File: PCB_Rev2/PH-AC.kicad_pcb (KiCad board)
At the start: 2 copper layers, 200 x 100 mm, 60 parts, among them J1 USB_C_Receptacle_USB2.0_14P, J2 Conn_01x03, Q1 DMG1012T, SW1 SW_Push, SW10 SW_Push, SW2 RotaryEncoder_Switch_MP, SW3 RotaryEncoder_Switch_MP, SW4 SW_Push, SW5 SW_Push, SW6 SW_Push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

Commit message: PCB Modification And Outfit Model Update
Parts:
- moved SW3 4.61 mm to (243.0, 65.6)
- moved SW2 4.24 mm to (77.0, 65.6)
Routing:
- net ENC2B: track 67.6 -> 62.8 mm
- net ENC2A: track 68.8 -> 64.1 mm
- net ENC1B: track 133.6 -> 129.4 mm
- net ENC1A: track 152.7 -> 151.0 mm
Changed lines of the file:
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@@
 	(footprint "Rotary_Encoder:RotaryEncoder_Alps_EC11E-Switch_Vertical_H20mm"
 		(layer "F.Cu")
-		(at 246.5 62.6)
+		(at 243 65.6)
 		(descr "Alps rotary encoder, EC12E... with switch, vertical shaft, http://www.alps.com/prod/info/E/HTML/Encoder/Incremental/EC11/EC11E15204A3.html")
 		(tags "rotary encoder")
@@
 	(footprint "Rotary_Encoder:RotaryEncoder_Alps_EC11E-Switch_Vertical_H20mm"
 		(layer "F.Cu")
-		(at 74 62.6)
+		(at 77 65.6)
 		(descr "Alps rotary encoder, EC12E... with switch, vertical shaft, http://www.alps.com/prod/info/E/HTML/Encoder/Incremental/EC11/EC11E15204A3.html")
 		(tags "rotary encoder")
@@
 	)
 	(segment
-		(start 191.7 77.1)
-		(end 156.35 77.1)
-		(width 0.2)
-		(layer "F.Cu")
-		(net 37)
-	)
-	(segment
-		(start 152.475 73.225)
-		(end 79.625 73.225)
-		(width 0.2)
-		(layer "F.Cu")
-		(net 37)
-	)
-	(segment
-		(start 156.35 77.1)
-		(end 152.475 73.225)
+		(start 198.075735 70.724265)
+		(end 191.7 77.1)
 		(width 0.2)
 		(layer "F.Cu")
@@
 	)
 	(segment
-		(start 198.075735 70.724265)
-		(end 191.7 77.1)
+		(start 198.924265 70.724265)
+		(end 198.075735 70.724265)
 		(width 0.2)
 		(layer "F.Cu")
@@
 	)
 	(segment
-		(start 79.625 73.225)
-		(end 74 67.6)
+		(start 83.5 77.1)
+		(end 77 70.6)
 		(width 0.2)
 		(layer "F.Cu")
@@
 	)
 	(segment
-		(start 198.924265 70.724265)
-		(end 198.075735 70.724265)
+		(start 191.7 77.1)
+		(end 83.5 77.1)
 		(width 0.2)
 		(layer "F.Cu")
@@
 	)
 	(segment
-		(start 69.8 66.8)
-		(end 74 62.6)
+		(start 74.3 65.6)
+		(end 77 65.6)
 		(width 0.2)
 		(layer "F.Cu")
@@
 	)
 	(segment
-		(start 77.05 80.7)
-		(end 69.8 73.45)
+		(start 71.7 75.35)
+		(end 71.7 68.2)
 		(width 0.2)
 		(layer "F.Cu")
@@
 	)
 	(segment
-		(start 197.926471 73.426471)
-		(end 190.652942 80.7)
+		(start 190.652942 80.7)
+		(end 77.05 80.7)
 		(width 0.2)
 		(layer "F.Cu")
@@
 	)
 	(segment
-		(start 69.8 73.45)
-		(end 69.8 66.8)
+		(start 77.05 80.7)
+		(end 71.7 75.35)
 		(width 0.2)
 		(layer "F.Cu")
@@
 	)
 	(segment
-		(start 190.652942 80.7)
-		(end 77.05 80.7)
+		(start 197.926471 73.426471)
+		(end 190.652942 80.7)
+		(width 0.2)
+		(layer "F.Cu")
+		(net 38)
+	)
+	(segment
+		(start 71.7 68.2)
+		(end 74.3 65.6)
 		(width 0.2)
 		(layer "F.Cu")
@@
 	)
 	(segment
-		(start 198.35 69.884314)
-		(end 198.35 68.6875)
+		(start 224.4 83.9)
+		(end 242.7 65.6)
 		(width 0.2)
 		(layer "B.Cu")
@@
 	)
 	(segment
-		(start 245.7 62.6)
-		(end 224.4 83.9)
+		(start 198.35 69.884314)
+		(end 198.35 68.6875)
 		(width 0.2)
 		(layer "B.Cu")
@@
 	)
 	(segment
-		(start 246.5 62.6)
-		(end 245.7 62.6)
+		(start 242.7 65.6)
+		(end 243 65.6)
 		(width 0.2)
 		(layer "B.Cu")
@@
 	)
 	(segment
-		(start 246.5 67.6)
-		(end 241.3 67.6)
+		(start 224.6 84.3)
+		(end 238.3 70.6)
 		(width 0.2)
 		(layer "B.Cu")
@@
 	)
 	(segment
-		(start 241.3 67.6)
-		(end 224.6 84.3)
+		(start 197.95 69.71863)
+		(end 197.95 68.6875)
 		(width 0.2)
 		(layer "B.Cu")
@@
 	)
 	(segment
-		(start 197.95 69.71863)
-		(end 197.95 68.6875)
+		(start 196.45 71.21863)
+		(end 197.95 69.71863)
 		(width 0.2)
 		(layer "B.Cu")
@@
 	)
 	(segment
-		(start 196.45 71.21863)
-		(end 197.95 69.71863)
+		(start 238.3 70.6)
+		(end 243 70.6)
 		(width 0.2)
 		(layer "B.Cu")

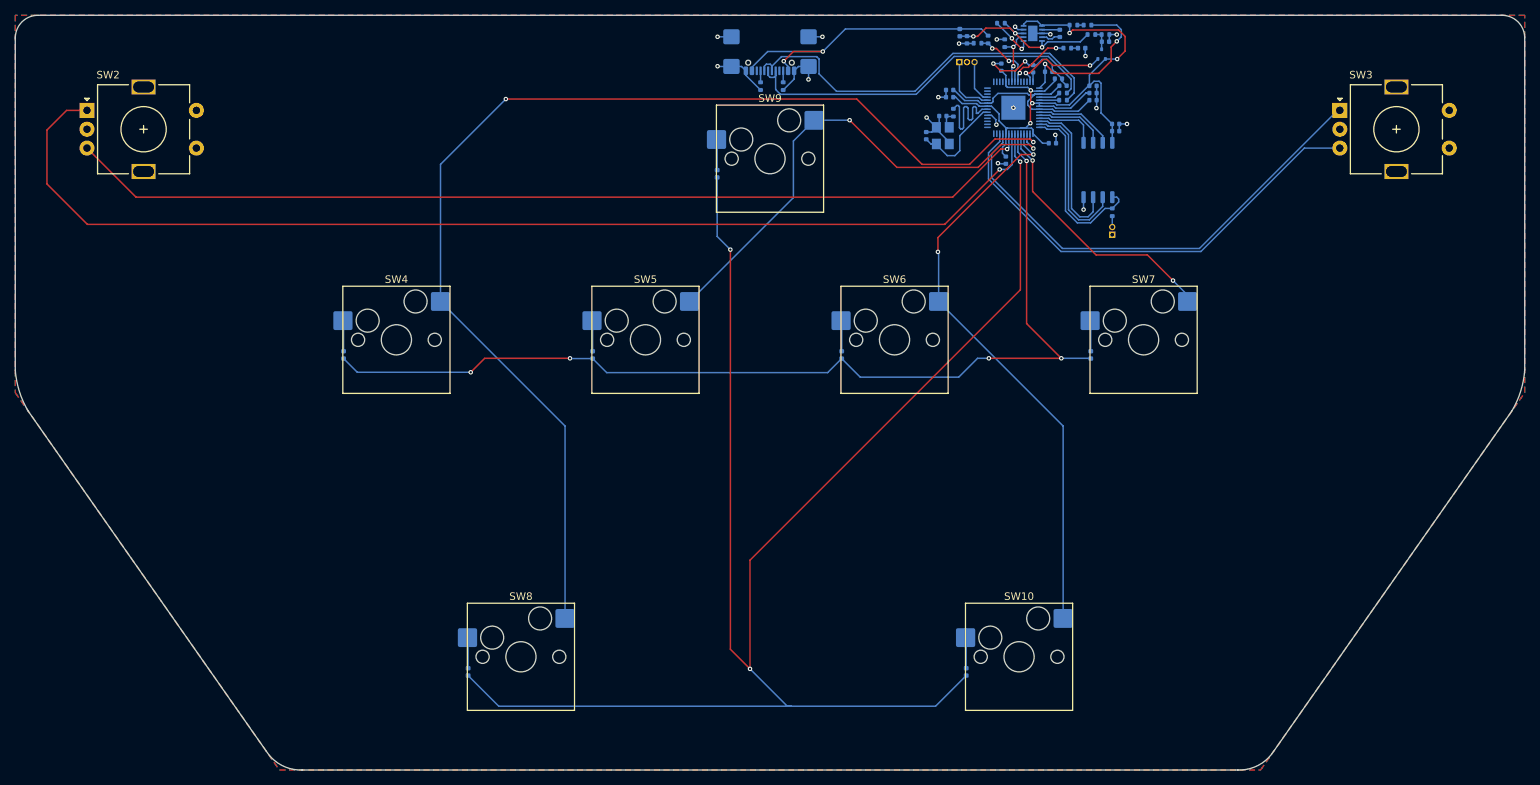
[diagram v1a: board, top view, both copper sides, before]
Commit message: Mouting Hole Adding
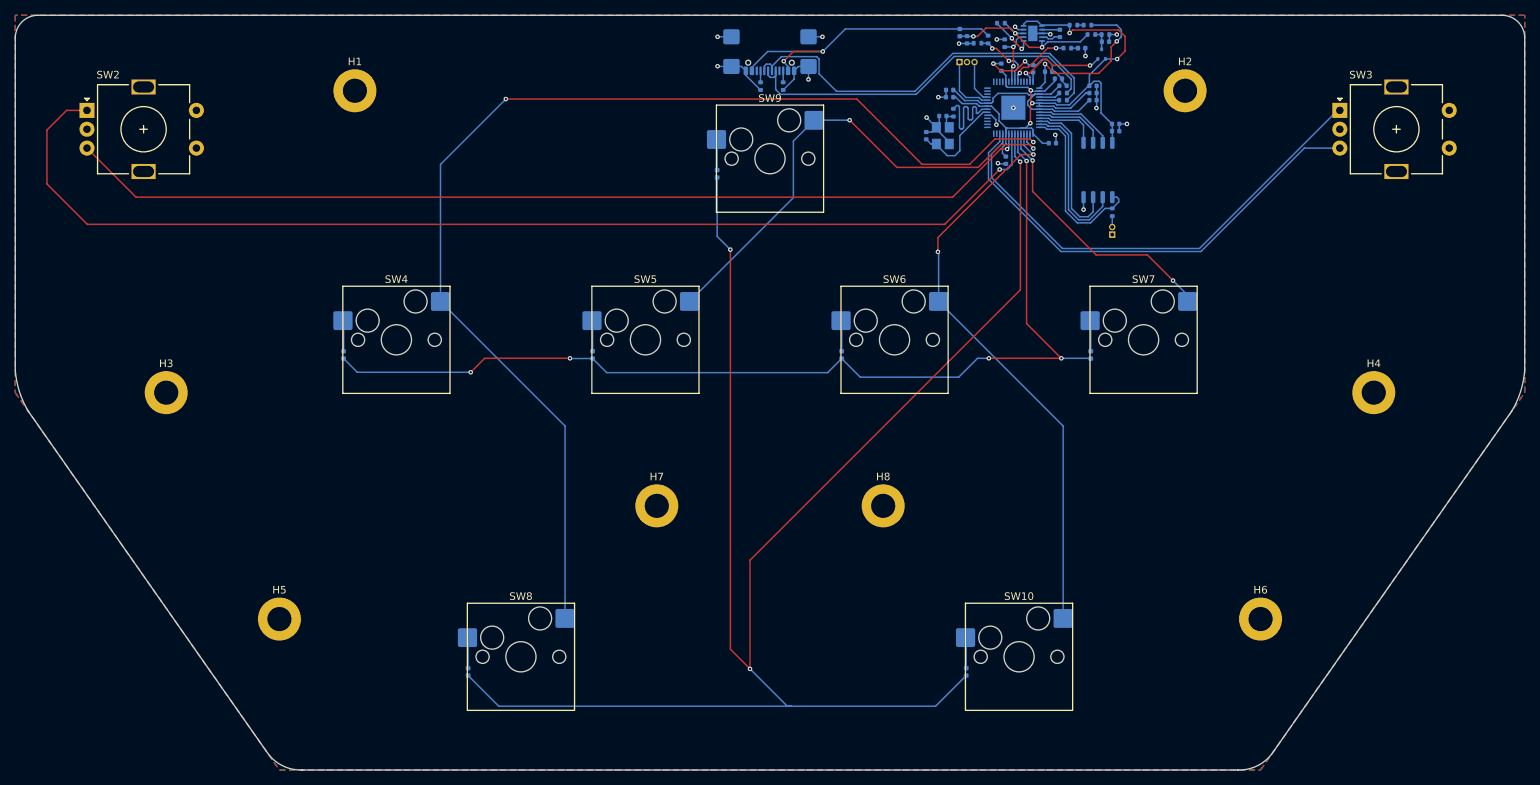
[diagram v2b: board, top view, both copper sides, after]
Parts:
- added H1: MountingHole, MountingHole:MountingHole_3.2mm_M3_ISO7380_Pad, F.Cu at (112.5, 63.0)
- added H2: MountingHole, MountingHole:MountingHole_3.2mm_M3_ISO7380_Pad, F.Cu at (222.5, 63.0)
- added H3: MountingHole, MountingHole:MountingHole_3.2mm_M3_ISO7380_Pad, F.Cu at (87.5, 103.0)
- added H4: MountingHole, MountingHole:MountingHole_3.2mm_M3_ISO7380_Pad, F.Cu at (247.5, 103.0)
- added H5: MountingHole, MountingHole:MountingHole_3.2mm_M3_ISO7380_Pad, F.Cu at (102.5, 133.0)
- added H6: MountingHole, MountingHole:MountingHole_3.2mm_M3_ISO7380_Pad, F.Cu at (232.5, 133.0)
- added H7: MountingHole, MountingHole:MountingHole_3.2mm_M3_ISO7380_Pad, F.Cu at (152.5, 118.0)
- added H8: MountingHole, MountingHole:MountingHole_3.2mm_M3_ISO7380_Pad, F.Cu at (182.5, 118.0)

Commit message: PCB Update
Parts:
- moved C11 1.90 mm to (204.4, 62.4)
- moved C15 1.90 mm to (213.3, 70.2)
- moved C18 1.90 mm to (190.4, 68.2)
- moved C2 1.90 mm to (210.3, 65.2)
- moved C7 1.90 mm to (210.3, 66.2)
- moved C9 1.90 mm to (206.3, 64.2)
- moved D1 1.90 mm to (192.7, 57.2)
- moved R1 1.90 mm to (209.6, 56.2)
- moved R10 1.90 mm to (210.1, 57.5)
- moved R11 1.90 mm to (211.9, 57.5)
- moved R2 1.90 mm to (207.7, 56.2)
- moved R3 1.90 mm to (206.3, 66.2)
- moved R4 1.90 mm to (206.3, 65.2)
- moved R7 1.90 mm to (198.1, 56.0)
- moved R9 1.90 mm to (212.8, 81.0)
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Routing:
- net /USB_DM: track 53.5 -> 49.0 mm
- net GND: track 62.9 -> 67.1 mm, vias 21 -> 23
- net ROW0: track 136.3 -> 134.4 mm
- net COL2: track 77.9 -> 76.0 mm
- net ROW1: track 229.8 -> 228.0 mm
- net +3V3: track 90.3 -> 91.6 mm
- net ENC1B: track 129.4 -> 128.6 mm
- net ENC1A: track 151.0 -> 150.2 mm
- net COL0: track 155.6 -> 156.3 mm
- net VBUS: track 41.5 -> 40.7 mm
- net COL3: track 35.4 -> 34.6 mm
- net COL1: track 66.3 -> 67.1 mm
- net /USB_DP: track 49.7 -> 49.0 mm

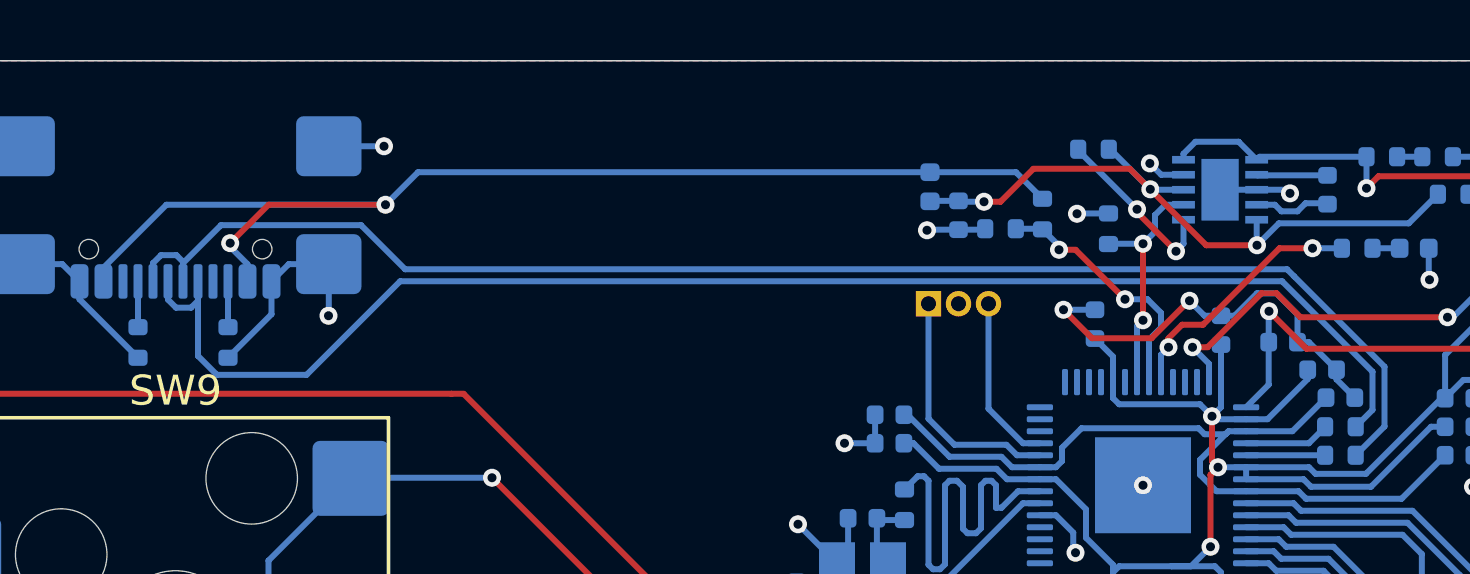
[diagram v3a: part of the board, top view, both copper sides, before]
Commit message: Component Package Modification
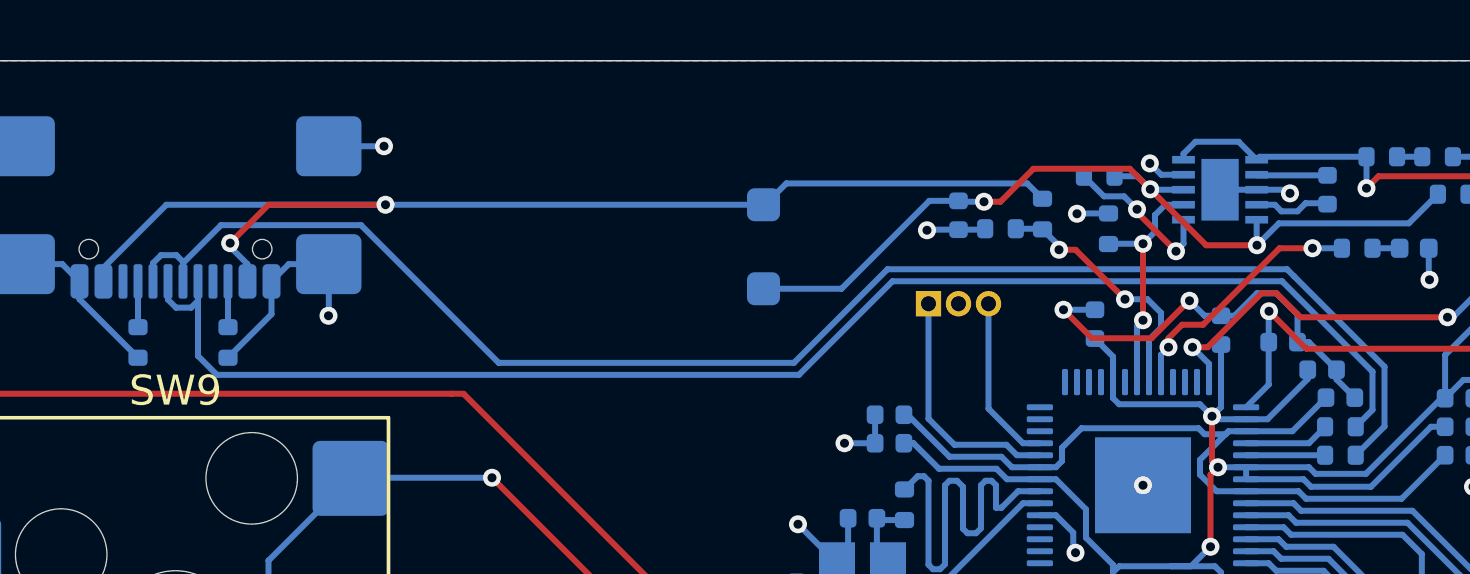
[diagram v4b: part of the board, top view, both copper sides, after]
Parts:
- D1: footprint Diode_SMD:D_0402_1005Metric -> Diode_SMD:D_SOD-123F
- moved D1 5.90 mm to (187.1, 59.2)
- moved R7 0.92 mm to (198.3, 56.9)
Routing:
- net /VSYS: track 23.1 -> 29.3 mm
- net /USB_DM: track 49.0 -> 51.5 mm
- net Net-(U2-EN): track 5.90 -> 5.32 mm
- added copper zone on B.Cu, net (none)
- removed copper zone on B.Cu, net +3V3
